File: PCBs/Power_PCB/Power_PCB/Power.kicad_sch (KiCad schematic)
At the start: 19 parts, among them J1 Conn_01x02, J12 Conn_01x04, J2 Conn_01x02, J3 Conn_01x02, Q1 SUD45P03-09, SW1 SW_Push_Open, U2 AMS1117-3.3, U5 TVS3300DRV

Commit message: Second iteration power board
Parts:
- removed J12: Conn_01x04, TerminalBlock:TerminalBlock_Altech_AK300-4_P5.00mm, symbol Connector_Generic:Conn_01x04
- removed SW1: SW_Push_Open, Button_Switch_THT:SW_Slide_SPDT_Straight_CK_OS102011MS2Q, symbol Switch:SW_Push_Open
- added J12: 8PCV-04-006, SHDR4W114P0X1112_1X4_4628X2032X1956P, symbol 8PCV-04-006:8PCV-04-006
- added S1: SLW-116641-5A-S-D, SLW1166415ASD, symbol SLW-116641-5A-S-D:SLW-116641-5A-S-D
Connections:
- net 14V8_IN: now also J12.4, S1.3 (NO)
- net EMERG_OUT: now also J3.1 (Pin_1), J12.2; no longer J3.2 (Pin_2)
- net GND: now also J12.3
- net RELAY_OUT: now also J12.1
- new net: J3.2 (Pin_2), S1.2 (COM)
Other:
- moved on the sheet: J3

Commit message: Power board revisions
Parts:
- removed S1: SLW-116641-5A-S-D, SLW1166415ASD, symbol SLW-116641-5A-S-D:SLW-116641-5A-S-D
- added S2: EGJ1210AAT2, EGJ1210AAT2, symbol EGJ1210AAT2:EGJ1210AAT2
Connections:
- net 14V8_IN: now also S2.2 (NO)
- net at J3.2 (Pin_2): now also S2.1 (COM)
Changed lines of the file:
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@@
 	(wire
 		(pts
-			(xy 88.9 110.49) (xy 99.06 110.49)
+			(xy 88.9 107.95) (xy 99.06 107.95)
 		)
 		(stroke
@@
 	(wire
 		(pts
-			(xy 204.47 50.8) (xy 220.98 50.8)
+			(xy 88.9 107.95) (xy 88.9 113.03)
 		)
 		(stroke
@@
 	(wire
 		(pts
-			(xy 88.9 110.49) (xy 88.9 113.03)
+			(xy 204.47 50.8) (xy 220.98 50.8)
 		)
 		(stroke
@@
 		(pts
 			(xy 153.67 97.79) (xy 151.13 97.79)
-		)
-		(stroke
-			(width 0)
-			(type default)
-		)
-	)
-	(wire
-		(pts
-			(xy 99.06 107.95) (xy 99.06 110.49)
 		)
 		(stroke
@@
 	)
 	(symbol
-		(lib_id "SLW-116641-5A-S-D:SLW-116641-5A-S-D")
-		(at 91.44 113.03 270)
-		(unit 1)
-		(exclude_from_sim no)
-		(in_bom yes)
-		(on_board yes)
-		(dnp no)
-		(fields_autoplaced yes)
-		(property "Reference" "S1"
-			(at 95.25 123.1899 90)
-			(effects
-				(font
-					(size 1.27 1.27)
-				)
-				(justify left)
-			)
-		)
-		(property "Value" "SLW-116641-5A-S-D"
-			(at 95.25 125.7299 90)
-			(effects
-				(font
-					(size 1.27 1.27)
-				)
-				(justify left)
-			)
-		)
-		(property "Footprint" "SLW1166415ASD"
-			(at -3.48 132.08 0)
-			(effects
-				(font
-					(size 1.27 1.27)
-				)
-				(justify left top)
-				(hide yes)
-			)
-		)
-		(property "Datasheet" "https://www.sameskydevices.com/product/resource/supplyframepdf/slw-116641-5a-s-d.pdf"
-			(at -103.48 132.08 0)
-			(effects
-				(font
-					(size 1.27 1.27)
-				)
-				(justify left top)
-				(hide yes)
-			)
-		)
-		(property "Description" "11.6 x 6 x 4.1 mm, 5 mm Raised Slide Actuator, Through Hole, Slide Switch"
-			(at 91.44 113.03 0)
-			(effects
-				(font
-					(size 1.27 1.27)
-				)
-				(hide yes)
-			)
-		)
-		(property "Height" "11.3"
-			(at -303.48 132.08 0)
-			(effects
-				(font
-					(size 1.27 1.27)
-				)
-				(justify left top)
-				(hide yes)
-			)
-		)
-		(property "Manufacturer_Name" "Same Sky"
-			(at -403.48 132.08 0)
-			(effects
-				(font
-					(size 1.27 1.27)
-				)
-				(justify left top)
-				(hide yes)
-			)
-		)
-		(property "Manufacturer_Part_Number" "SLW-116641-5A-S-D"
-			(at -503.48 132.08 0)
-			(effects
-				(font
-					(size 1.27 1.27)
-				)
-				(justify left top)
-				(hide yes)
-			)
-		)
-		(property "Mouser Part Number" "179-SLW1166415ASD"
-			(at -603.48 132.08 0)
-			(effects
-				(font
-					(size 1.27 1.27)
-				)
-				(justify left top)
-				(hide yes)
-			)
-		)
-		(property "Mouser Price/Stock" "https://www.mouser.co.uk/ProductDetail/Same-Sky/SLW-116641-5A-S-D?qs=IKkN%2F947nfBZSdW8n5Vqgw%3D%3D"
-			(at -703.48 132.08 0)
-			(effects
-				(font
-					(size 1.27 1.27)
-				)
-				(justify left top)
-				(hide yes)
-			)
-		)
-		(property "Arrow Part Number" "SLW-116641-5A-S-D"
-			(at -803.48 132.08 0)
-			(effects
-				(font
-					(size 1.27 1.27)
-				)
-				(justify left top)
-				(hide yes)
-			)
-		)
-		(property "Arrow Price/Stock" "https://www.arrow.com/en/products/slw-116641-5a-s-d/cui-devices?utm_currency=USD&region=nac"
-			(at -903.48 132.08 0)
-			(effects
-				(font
-					(size 1.27 1.27)
-				)
-				(justify left top)
-				(hide yes)
-			)
-		)
-		(pin "1"
-		)
-		(pin "3"
-		)
-		(pin "2"
-		)
-		(instances
-			(project ""
-				(path "/87325cad-d0d9-4e34-97c3-9178133a19b1/ceb728e0-0a2f-47f1-b8f2-8a2cf5487bda"
-					(reference "S1")
-					(unit 1)
-				)
-			)
-		)
-	)
-	(symbol
 		(lib_id "Diode:1N4148")
 		(at 118.11 121.92 270)
@@
 					(unit 1)
 				)
+			)
+		)
+	)
+	(symbol
+		(lib_id "EGJ1210AAT2:EGJ1210AAT2")
+		(at 86.36 113.03 90)
+		(mirror x)
+		(unit 1)
+		(exclude_from_sim no)
+		(in_bom yes)
+		(on_board yes)
+		(dnp no)
+		(property "Reference" "S2"
+			(at 82.55 123.1899 90)
+			(effects
+				(font
+					(size 1.27 1.27)
+				)
+				(justify left)
+			)
+		)
+		(property "Value" "EGJ1210AAT2"
+			(at 82.55 125.7299 90)
+			(effects
+				(font
+					(size 1.27 1.27)
+				)
+				(justify left)
+			)
+		)
+		(property "Footprint" "EGJ1210AAT2"
+			(at 181.28 132.08 0)
+			(effects
+				(font
+					(size 1.27 1.27)
+				)
+				(justify left top)
+				(hide yes)
+			)
+		)
+		(property "Datasheet" "https://configured-product-images.s3.amazonaws.com/2D/specs/EGJ1210AAT2.pdf"
+			(at 281.28 132.08 0)
+			(effects
+				(font
+					(size 1.27 1.27)
+				)
+				(justify left top)
+				(hide yes)
+			)
+		)
+		(property "Description" "SLIDE, 300mA / 500mA, 24VDC / 12VDC SPDT, On-On Through Hole, Right Angle"
+			(at 86.36 113.03 0)
+			(effects
+				(font
+					(size 1.27 1.27)
+				)
+				(hide yes)
+			)
+		)
+		(property "Height" "2.75"
+			(at 481.28 132.08 0)
+			(effects
+				(font
+					(size 1.27 1.27)
+				)
+				(justify left top)
+				(hide yes)
+			)
+		)
+		(property "Manufacturer_Name" "E-Switch"
+			(at 581.28 132.08 0)
+			(effects
+				(font
+					(size 1.27 1.27)
+				)
+				(justify left top)
+				(hide yes)
+			)
+		)
+		(property "Manufacturer_Part_Number" "EGJ1210AAT2"
+			(at 681.28 132.08 0)
+			(effects
+				(font
+					(size 1.27 1.27)
+				)
+				(justify left top)
+				(hide yes)
+			)
+		)
+		(property "Mouser Part Number" "612-EGJ1210AAT2"
+			(at 781.28 132.08 0)
+			(effects
+				(font
+					(size 1.27 1.27)
+				)
+				(justify left top)
+				(hide yes)
+			)
+		)
+		(property "Mouser Price/Stock" "https://www.mouser.co.uk/ProductDetail/E-Switch/EGJ1210AAT2?qs=%252BXxaIXUDbq28DPumZsnIIA%3D%3D"
+			(at 881.28 132.08 0)
+			(effects
+				(font
+					(size 1.27 1.27)
+				)
+				(justify left top)
+				(hide yes)
+			)
+		)
+		(property "Arrow Part Number" ""
+			(at 981.28 132.08 0)
+			(effects
+				(font
+					(size 1.27 1.27)
+				)
+				(justify left top)
+				(hide yes)
+			)
+		)
+		(property "Arrow Price/Stock" ""
+			(at 1081.28 132.08 0)
+			(effects
+				(font
+					(size 1.27 1.27)
+				)
+				(justify left top)
+				(hide yes)
+			)
+		)
+		(pin "1"
+		)
+		(pin "2"
+		)
+		(pin "3"
+		)
+		(instances
+			(project ""
+				(path "/87325cad-d0d9-4e34-97c3-9178133a19b1/ceb728e0-0a2f-47f1-b8f2-8a2cf5487bda"
+					(reference "S2")
+					(unit 1)
+				)

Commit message: follow up meeting changes
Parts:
- removed J12: 8PCV-04-006, SHDR4W114P0X1112_1X4_4628X2032X1956P, symbol 8PCV-04-006:8PCV-04-006
- added J12: Conn_01x02, TerminalBlock:TerminalBlock_Altech_AK300-2_P5.00mm, symbol Connector_Generic:Conn_01x02
- added J18: 8PCV-02-006, 8PCV02006, symbol 8PCV-02-006:8PCV-02-006
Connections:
- net 14V8_IN: now also J18.2
- net EMERG_OUT: now also J12.1 (Pin_1)
- net GND: now also J12.2 (Pin_2)
- net RELAY_OUT: now also J18.1

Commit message: Modified output connectors to female
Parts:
- J18: footprint 8PCV02006 -> iprl_footprints:8PCV02006
- S2: footprint EGJ1210AAT2 -> iprl_footprints:EGJ1210AAT2
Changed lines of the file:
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@@
 			)
 		)
-		(property "Footprint" "EGJ1210AAT2"
+		(property "Footprint" "iprl_footprints:EGJ1210AAT2"
 			(at 181.28 132.08 0)
 			(effects
@@
 			)
 		)
-		(property "Footprint" "8PCV02006"
+		(property "Footprint" "iprl_footprints:8PCV02006"
 			(at 48.59 76.2 0)
 			(effects

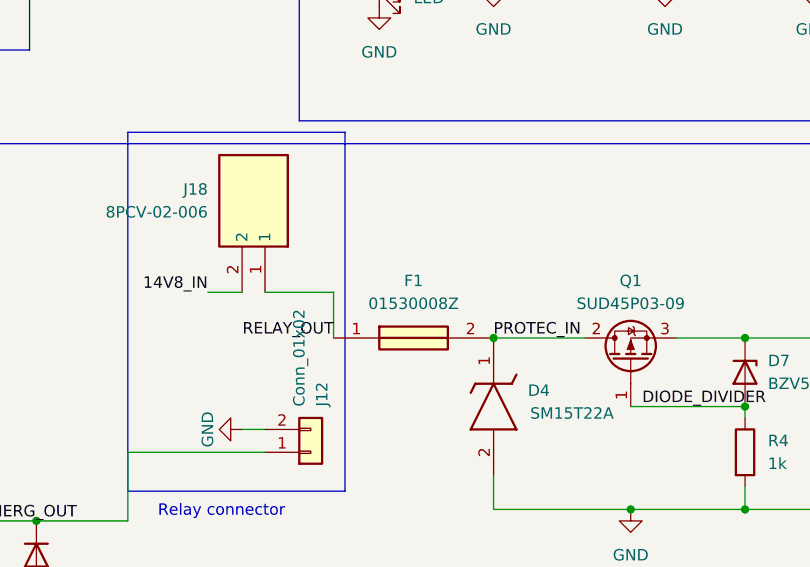
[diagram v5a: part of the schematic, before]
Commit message: Replaced fuse holders with 01000064Z
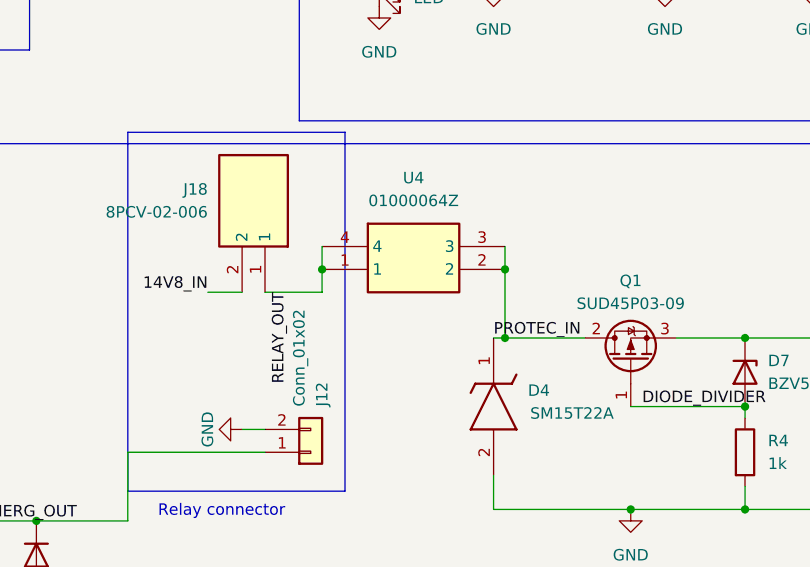
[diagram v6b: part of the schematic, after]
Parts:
- removed F1: 01530008Z, iprl_footprints:01530008, symbol 01530008Z:01530008Z
- added U4: 01000064Z, 01000064Z, symbol 01000064Z:01000064Z
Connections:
- net PROTEC_IN: now also U4.2, U4.3
- net RELAY_OUT: now also U4.1, U4.4
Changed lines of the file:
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@@
-	)
-	(junction
-		(at 168.91 97.79)
-		(diameter 0)
-		(color 0 0 0 0)
 	)
 	(junction
@@
 	)
 	(junction
+		(at 170.18 90.17)
+		(diameter 0)
+		(color 0 0 0 0)
+	)
+	(junction
 		(at 226.06 97.79)
+		(diameter 0)
+		(color 0 0 0 0)
+	)
+	(junction
+		(at 170.18 97.79)
 		(diameter 0)
 		(color 0 0 0 0)
@@
 	)
 	(junction
+		(at 149.86 90.17)
+		(diameter 0)
+		(color 0 0 0 0)
+	)
+	(junction
 		(at 204.47 50.8)
 		(diameter 0)
@@
 	(wire
 		(pts
-			(xy 143.51 92.71) (xy 151.13 92.71)
+			(xy 143.51 92.71) (xy 149.86 92.71)
 		)
 		(stroke
@@
 	(wire
 		(pts
+			(xy 170.18 87.63) (xy 170.18 90.17)
+		)
+		(stroke
+			(width 0)
+			(type default)
+		)
+	)
+	(wire
+		(pts
 			(xy 184.15 105.41) (xy 196.85 105.41)
 		)
@@
 	(wire
 		(pts
+			(xy 170.18 90.17) (xy 170.18 97.79)
+		)
+		(stroke
+			(width 0)
+			(type default)
+		)
+	)
+	(wire
+		(pts
 			(xy 195.58 50.8) (xy 204.47 50.8)
 		)
@@
 	(wire
 		(pts
+			(xy 170.18 97.79) (xy 179.07 97.79)
+		)
+		(stroke
+			(width 0)
+			(type default)
+		)
+	)
+	(wire
+		(pts
 			(xy 226.06 116.84) (xy 226.06 113.03)
 		)
@@
 	(wire
 		(pts
-			(xy 168.91 97.79) (xy 179.07 97.79)
+			(xy 168.91 97.79) (xy 170.18 97.79)
 		)
 		(stroke
@@
 	(wire
 		(pts
+			(xy 149.86 90.17) (xy 149.86 92.71)
+		)
+		(stroke
+			(width 0)
+			(type default)
+		)
+	)
+	(wire
+		(pts
 			(xy 101.6 107.95) (xy 101.6 113.03)
 		)
@@
 	(wire
 		(pts
-			(xy 151.13 92.71) (xy 151.13 97.79)
-		)
-		(stroke
-			(width 0)
-			(type default)
-		)
-	)
-	(wire
-		(pts
 			(xy 88.9 107.95) (xy 88.9 113.03)
 		)
@@
 		(pts
 			(xy 189.23 97.79) (xy 196.85 97.79)
+		)
+		(stroke
+			(width 0)
+			(type default)
+		)
+	)
+	(wire
+		(pts
+			(xy 149.86 87.63) (xy 149.86 90.17)
 		)
 		(stroke
@@
 	)
 	(label "RELAY_OUT"
-		(at 151.13 97.79 180)
+		(at 146.05 92.71 270)
 		(effects
 			(font
@@
 	)
 	(symbol
+		(lib_id "01000064Z:01000064Z")
+		(at 149.86 87.63 0)
+		(unit 1)
+		(exclude_from_sim no)
+		(in_bom yes)
+		(on_board yes)
+		(dnp no)
+		(fields_autoplaced yes)
+		(property "Reference" "U4"
+			(at 160.02 80.01 0)
+			(effects
+				(font
+					(size 1.27 1.27)
+				)
+			)
+		)
+		(property "Value" "01000064Z"
+			(at 160.02 82.55 0)
+			(effects
+				(font
+					(size 1.27 1.27)
+				)
+			)
+		)
+		(property "Footprint" "01000064Z"
+			(at 166.37 182.55 0)
+			(effects
+				(font
+					(size 1.27 1.27)
+				)
+				(justify left top)
+				(hide yes)
+			)
+		)
+		(property "Datasheet" "https://m.littelfuse.com/~/media/electronics/datasheets/fuse_clips/littelfuse_fuseclip_100_datasheet.pdf.pdf"
+			(at 166.37 282.55 0)
+			(effects
+				(font
+					(size 1.27 1.27)
+				)
+				(justify left top)
+				(hide yes)
+			)
+		)
+		(property "Description" "Fuse Holder HIGH PROF. BLOCK MINI FUSE THT 30 AMP."
+			(at 149.86 87.63 0)
+			(effects
+				(font
+					(size 1.27 1.27)
+				)
+				(hide yes)
+			)
+		)
+		(property "Height" "7.37"
+			(at 166.37 482.55 0)
+			(effects
+				(font
+					(size 1.27 1.27)
+				)
+				(justify left top)
+				(hide yes)
+			)
+		)
+		(property "Manufacturer_Name" "LITTELFUSE"
+			(at 166.37 582.55 0)
+			(effects
+				(font
+					(size 1.27 1.27)
+				)
+				(justify left top)
+				(hide yes)
+			)
+		)
+		(property "Manufacturer_Part_Number" "01000064Z"
+			(at 166.37 682.55 0)
+			(effects
+				(font
+					(size 1.27 1.27)
+				)
+				(justify left top)
+				(hide yes)
+			)
+		)
+		(property "Mouser Part Number" "576-01000064Z"
+			(at 166.37 782.55 0)
+			(effects
+				(font
+					(size 1.27 1.27)
+				)
+				(justify left top)
+				(hide yes)
+			)
+		)
+		(property "Mouser Price/Stock" "https://www.mouser.co.uk/ProductDetail/Littelfuse/01000064Z?qs=pUKx8fyJudDk0mp%2FixA2Uw%3D%3D"
+			(at 166.37 882.55 0)
+			(effects
+				(font
+					(size 1.27 1.27)
+				)
+				(justify left top)
+				(hide yes)
+			)
+		)
+		(property "Arrow Part Number" ""
+			(at 166.37 982.55 0)
+			(effects
+				(font
+					(size 1.27 1.27)
+				)
+				(justify left top)
+				(hide yes)
+			)
+		)
+		(property "Arrow Price/Stock" ""
+			(at 166.37 1082.55 0)
+			(effects
+				(font
+					(size 1.27 1.27)
+				)
+				(justify left top)
+				(hide yes)
+			)
+		)
+		(pin "3"
+		)
+		(pin "4"
+		)
+		(pin "2"
+		)
+		(pin "1"
+		)
+		(instances
+			(project ""
+				(path "/87325cad-d0d9-4e34-97c3-9178133a19b1/ceb728e0-0a2f-47f1-b8f2-8a2cf5487bda"
+					(reference "U4")
+					(unit 1)
+				)
+			)
+		)
+	)
+	(symbol
 		(lib_id "Device:LED")
 		(at 220.98 62.23 90)
@@
 					(unit 1)
 				)
-			)
-		)
-	)
-	(symbol
-		(lib_id "01530008Z:01530008Z")
-		(at 151.13 97.79 0)
-		(unit 1)
-		(exclude_from_sim no)
-		(in_bom yes)
-		(on_board yes)
-		(dnp no)
-		(fields_autoplaced yes)
-		(property "Reference" "F1"
-			(at 160.02 91.44 0)
-			(effects
-				(font
-					(size 1.27 1.27)
-				)
-			)
-		)
-		(property "Value" "01530008Z"
-			(at 160.02 93.98 0)
-			(effects
-				(font
-					(size 1.27 1.27)
-				)
-			)
-		)
-		(property "Footprint" "iprl_footprints:01530008"
-			(at 165.1 193.98 0)
-			(effects
-				(font
-					(size 1.27 1.27)
-				)
-				(justify left top)
-				(hide yes)
-			)
-		)
-		(property "Datasheet" "http://www.littelfuse.com/data/en/data_sheets/153_pcmount.pdf"
-			(at 165.1 293.98 0)
-			(effects
-				(font
-					(size 1.27 1.27)
-				)
-				(justify left top)
-				(hide yes)
-			)
-		)
-		(property "Description" "Mini fuseholder,15A 32V Littelfuse 15A PCB Mount Fuse Holder Automotive Fuse, 32 V"
-			(at 151.13 97.79 0)
-			(effects
-				(font
-					(size 1.27 1.27)
-				)
-				(hide yes)
-			)
-		)
-		(property "Height" ""
-			(at 165.1 493.98 0)
-			(effects
-				(font
-					(size 1.27 1.27)
-				)
-				(justify left top)
-				(hide yes)
-			)
-		)
-		(property "Mouser Part Number" "576-01530008Z"
-			(at 165.1 593.98 0)
-			(effects
-				(font
-					(size 1.27 1.27)
-				)
-				(justify left top)
-				(hide yes)
-			)
-		)
-		(property "Mouser Price/Stock" "https://www.mouser.co.uk/ProductDetail/Littelfuse/01530008Z?qs=gu7KAQ731UQHzmSA1Of2BQ%3D%3D"
-			(at 165.1 693.98 0)
-			(effects
-				(font
-					(size 1.27 1.27)
-				)
-				(justify left top)
-				(hide yes)
-			)
-		)
-		(property "Manufacturer_Name" "LITTELFUSE"
-			(at 165.1 793.98 0)
-			(effects
-				(font
-					(size 1.27 1.27)
-				)
-				(justify left top)
-				(hide yes)
-			)
-		)
-		(property "Manufacturer_Part_Number" "01530008Z"
-			(at 165.1 893.98 0)
-			(effects
-				(font
-					(size 1.27 1.27)
-				)
-				(justify left top)
-				(hide yes)
-			)
-		)
-		(pin "2"
-		)
-		(pin "1"
-		)
-		(instances
-			(project ""
-				(path "/87325cad-d0d9-4e34-97c3-9178133a19b1/ceb728e0-0a2f-47f1-b8f2-8a2cf5487bda"
-					(reference "F1")
-					(unit 1)
-				)
-				(path "/87325cad-d0d9-4e34-97c3-9178133a19b1/ee5313ea-497a-4c98-8204-4918f1d5ff09"
-					(reference "F1")
-					(unit 1)
-				)

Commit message: submitted power board
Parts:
- removed D1: 1N4148, Diode_THT:D_DO-35_SOD27_P7.62mm_Horizontal, symbol Diode:1N4148
- removed J18: 8PCV-02-006, iprl_footprints:8PCV02006, symbol 8PCV-02-006:8PCV-02-006
- removed Q1: SUD45P03-09, Package_TO_SOT_SMD:TO-252-2, symbol Transistor_FET:SUD45P03-09
- removed S2: EGJ1210AAT2, iprl_footprints:EGJ1210AAT2, symbol EGJ1210AAT2:EGJ1210AAT2
- removed U2: AMS1117-3.3, Package_TO_SOT_SMD:SOT-223-3_TabPin2, symbol Regulator_Linear:AMS1117-3.3
- removed U4: 01000064Z, 01000064Z, symbol 01000064Z:01000064Z
- added D1: 1N4148WT, SODFL1608X70N, symbol 1N4148WT:1N4148WT
- added J18: YK4420203000G, RHDR2W120P0X950_1X2_2050X1430X1790P, symbol YK4420203000G:YK4420203000G
- added Q4: NTD25P03LT4G, iprl_footprints:MJD45H11T4G, symbol NTD25P03LT4G:NTD25P03LT4G
- added S1: SK12F14G5, SK12F14G5, symbol SK12F14G5:SK12F14G5
- added U4: 178.6164.0001, 178.6164.XXX1, symbol 178_6164_0001:178.6164.0001
- added U9: AMS1117-3.3, Package_TO_SOT_SMD:SOT-223-3_TabPin2, symbol Regulator_Linear:AMS1117-3.3
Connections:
- net +3.3V: now also U9.2 (VO)
- net +5V: now also U9.3 (VI)
- net 14V8_IN: now also J18.1, S1.3 (NO)
- net 14V8_PROTECTED: now also Q4.3 (S)
- net DIODE_DIVIDER: now also Q4.1 (G)
- net EMERG_OUT: now also D1.1 (K)
- net GND: now also D1.2 (A), U9.1 (GND)
- net PROTEC_IN: now also Q4.2 (D), U4.2
- net RELAY_OUT: now also J18.2, U4.1
- net at J3.2 (Pin_2): now also S1.2 (COM)
- no-connect marks 0 -> 2
